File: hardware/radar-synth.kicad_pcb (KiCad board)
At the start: 4 copper layers, 50 x 40 mm, 75 parts, among them J3 Conn_Coaxial_Small, J4 Conn_Coaxial_Small, J5 Conn_Coaxial_Small, J6 Conn_01x06_MountingPin, U1 74AUP1G34, U2 LMX2572RHAT, U3 XIAO-ESP32S3-PLUS, U4 74AUP1G04, U5 Si570, U6 PL133-27GC-R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

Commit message: Ready for FAB info
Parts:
- added C38: 100n, Capacitor_SMD:C_0402_1005Metric, F.Cu at (143.2, 62.2)
- added C39: 1u, Capacitor_SMD:C_0402_1005Metric, F.Cu at (142.1, 62.2)
- added C40: 100n, Capacitor_SMD:C_0402_1005Metric, F.Cu at (172.7, 94.8)
- added C41: 1u, Capacitor_SMD:C_0402_1005Metric, F.Cu at (172.7, 95.9)
- added FB4: 180R, Inductor_SMD:L_0402_1005Metric, F.Cu at (144.6, 61.8)
- added G***: LOGO, footprint:paw, F.Cu at (166.4, 67.6)
- added H1: MountingHole, MountingHole:MountingHole_2.7mm_M2.5, F.Cu at (139.0, 55.0)
- added H2: MountingHole, MountingHole:MountingHole_2.7mm_M2.5, F.Cu at (181.0, 55.0)
- added H3: MountingHole, MountingHole:MountingHole_2.7mm_M2.5, F.Cu at (181.0, 103.0)
- added H4: MountingHole, MountingHole:MountingHole_2.7mm_M2.5, F.Cu at (139.0, 103.0)
- added TP1: TestPoint, TestPoint:TestPoint_THTPad_1.0x1.0mm_Drill0.5mm, F.Cu at (161.5, 70.1)
- added TP2: TestPoint, TestPoint:TestPoint_THTPad_1.0x1.0mm_Drill0.5mm, F.Cu at (166.7, 91.0)
- R18, R19, R2: moved to B.Cu
- moved C3 31.1 mm to (168.6, 94.8)
- moved FB2 29.7 mm to (169.1, 93.1), turned to 90 degrees
- moved C4 29.6 mm to (168.6, 95.9), turned to 180 degrees
- moved FB3 27.5 mm to (172.3, 93.2), turned to 90 degrees
- moved R19 17.8 mm to (149.4, 79.6), turned to 90 degrees
- moved R18 17.6 mm to (152.0, 79.5), turned to 90 degrees
- moved R20 4.44 mm to (151.2, 74.6)
- moved R2 2.10 mm to (140.0, 96.8), turned to 180 degrees
- moved D2 0.30 mm to (138.5, 96.8)
- moved R26 0.12 mm to (157.0, 72.5)
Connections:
- net 3V3_RF renamed 3V3_OSC
- net Net-(J6-Pin_1) renamed /J6_5V_EXT
- U2 pad V: (no net) -> GND
- U3 pad 10: /controller/i2c0.scl -> /controller/ref_clk_select
- U3 pad 21: /controller/ref_clk_en -> /controller/i2c0.scl
- U3 pad 22: /controller/ref_clk_select -> /controller/i2c0.sda
- U3 pad 9: /controller/i2c0.sda -> /controller/ref_clk_en
- U5 pad 7: /ref_osc/i2c.sda -> /controller/i2c0.sda
- U5 pad 8: /ref_osc/i2c.scl -> /controller/i2c0.scl
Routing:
- net /controller/ref_clk_select: track 0.00 -> 31.3 mm, vias 0 -> 2
- net /lmx2572_rf_pll_synth/REF_OSC_P: track 0.01 -> 30.3 mm
- net Net-(U2-VTUNE): track 1.92 -> 31.3 mm, vias 0 -> 2
- net /J6_5V_EXT: track 0.00 -> 20.8 mm, vias 0 -> 2
- net 3V3: track 2.29 -> 19.2 mm, vias 0 -> 9
- net /controller/i2c0.scl: track 0.00 -> 14.4 mm, vias 0 -> 1
- net /controller/i2c0.sda: track 0.00 -> 13.8 mm, vias 0 -> 1
- net Net-(C31-Pad2): track 1.31 -> 15.0 mm, vias 0 -> 2
- net Net-(U2-SYNC): track 4.44 -> 17.3 mm
- net /controller/ref_clk_en: track 0.00 -> 4.90 mm
- net /controller/LED0: track 0.00 -> 4.05 mm
- net /controller/lmx2572.muxout: track 32.5 -> 36.0 mm
- net Net-(U5-CLK+): track 0.00 -> 3.28 mm
- net 3V3_OSC: track 9.80 -> 13.1 mm, vias 0 -> 5
- net /controller/lmx2572.ce: track 31.4 -> 34.6 mm
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- added copper zone on In2.Cu, net /J6_5V_EXT
- added copper zone on In2.Cu, net 3V3
- added copper zone on In2.Cu, net 3V3_OSC
- added copper zone on In2.Cu, net 3V3_PLL
- added copper zone on In2.Cu, net 3V3_PLL_RF
- added copper zone on B.Cu, net GND
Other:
- board size 50 x 40 mm -> 50 x 56 mm
- board text added: "${DATE}"
- board text added: "${PROJECT}"
- board text added: "1"
- board text added: "15"
- board text added: "16"
- board text added: "17"
- board text added: "18"
- board text added: "19"
- board text added: "2"
- board text added: "20"
- board text added: "3"
- board text added: "3V3"
- board text added: "3V3_PLL"
- board text added: "3V3_PLL_RF"
- board text added: "4"
- board text added: "5"
- board text added: "5V0"
- board text added: "6"
- board text added: "7"
- board text added: "CE"
- board text added: "CSB"
- board text added: "G"
- board text added: "GND"
- board text added: "OSC"
- board text added: "RAMPCLK"
- board text added: "RAMPDIR"
- board text added: "REF-CLK-EN"
- board text added: "REF-CLK-SELECT"
- board text added: "REFOSC"
- board text added: "REV: ${REVISION}"
- board text added: "RFA"
- board text added: "RFB"
- board text added: "RXD0"
- board text added: "S/N"
- board text added: "SCK"
- board text added: "SCL"
- board text added: "SDA"
- board text added: "SDI"
- board text added: "SDO"
- board text added: "SYNC"
- board text added: "SYSREF"
- board text added: "SysREF"
- board text added: "TXD0"
- board text added: "VBUS"
- board text added: "Vtune"

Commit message: Sent off for quote
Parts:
- removed G***: LOGO, footprint:paw
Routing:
- net GND: vias 261 -> 280
- added copper zone on In2.Cu, net GND
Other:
- board text added: "${CURRENT_DATE}"
- board text added: "${ISSUE_DATE}"
- board text added: "${REVISION}"
- board text added: "BOTTOM ASSEMBLY FOR ${PROJECT}"
- board text added: "TOP ASSEMBLY DIAGRAM FOR ${PROJECT}"
- board text removed: "REV: ${REVISION}"
- board text removed: "S/N"

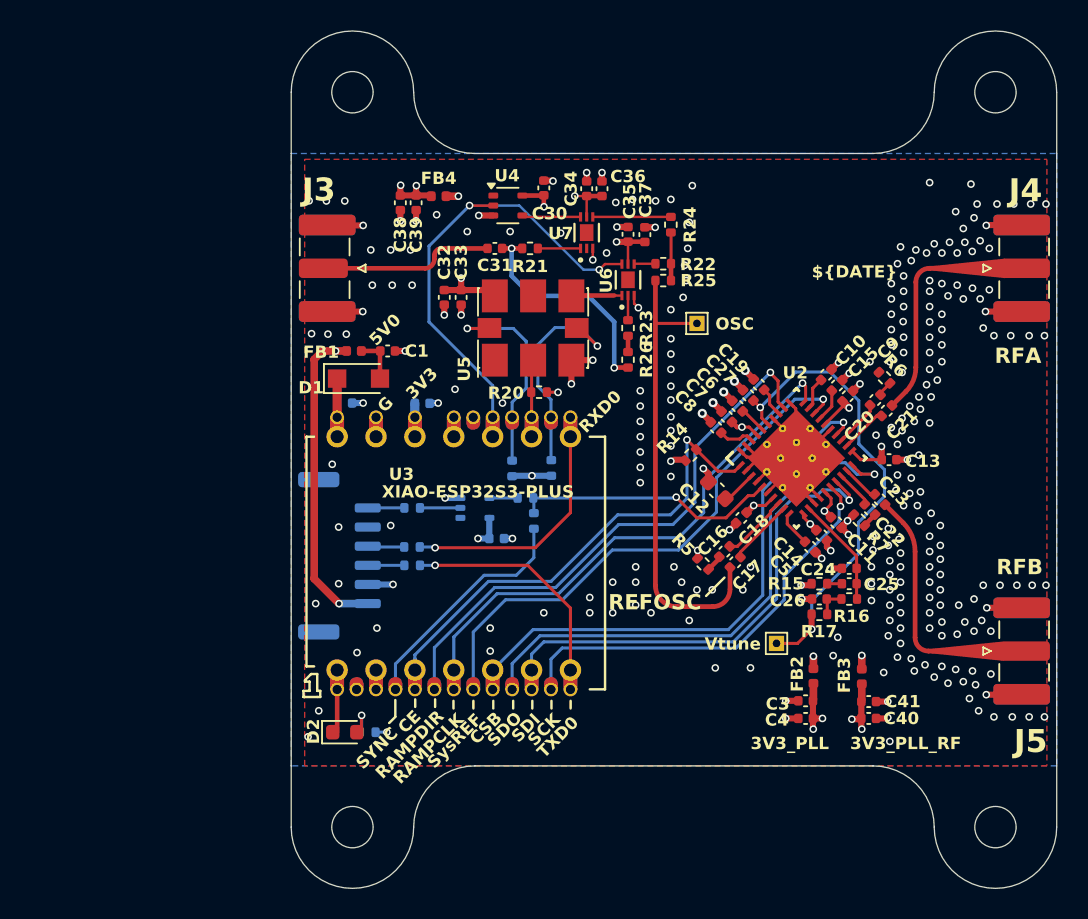
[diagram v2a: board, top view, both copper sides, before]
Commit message: Fixed silkscreen and re-submitted
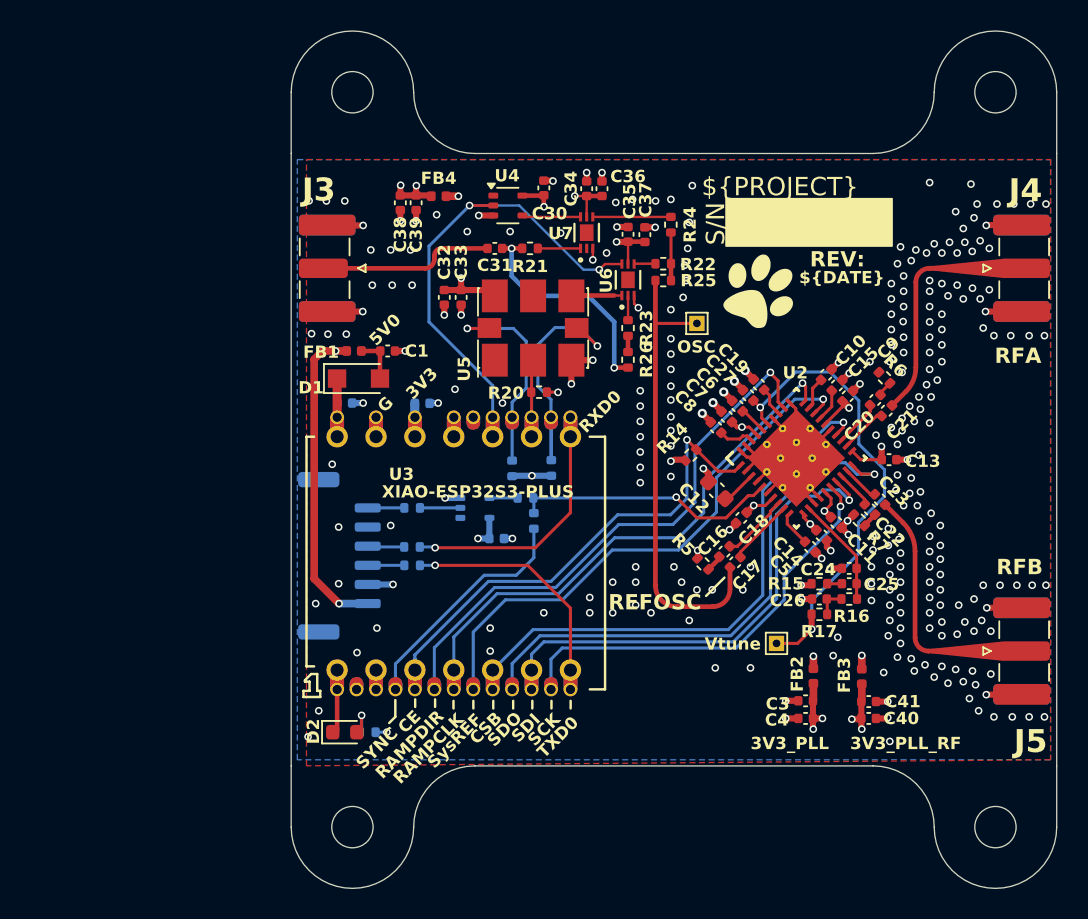
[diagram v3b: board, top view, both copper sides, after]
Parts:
- added G***: LOGO, footprint:paw, F.Cu at (165.6, 68.0)
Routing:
- net /controller/i2c0.scl: track 14.4 -> 17.2 mm
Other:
- board text added: "REV: ${REVISION}"
- board text added: "S/N"
